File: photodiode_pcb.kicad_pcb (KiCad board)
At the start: 2 copper layers, 11.7 x 30.2 mm, 15 parts, among them P1 CONN_01X04, U1 LTC2461, U3 SD100-13-23-222, U4 OPA381

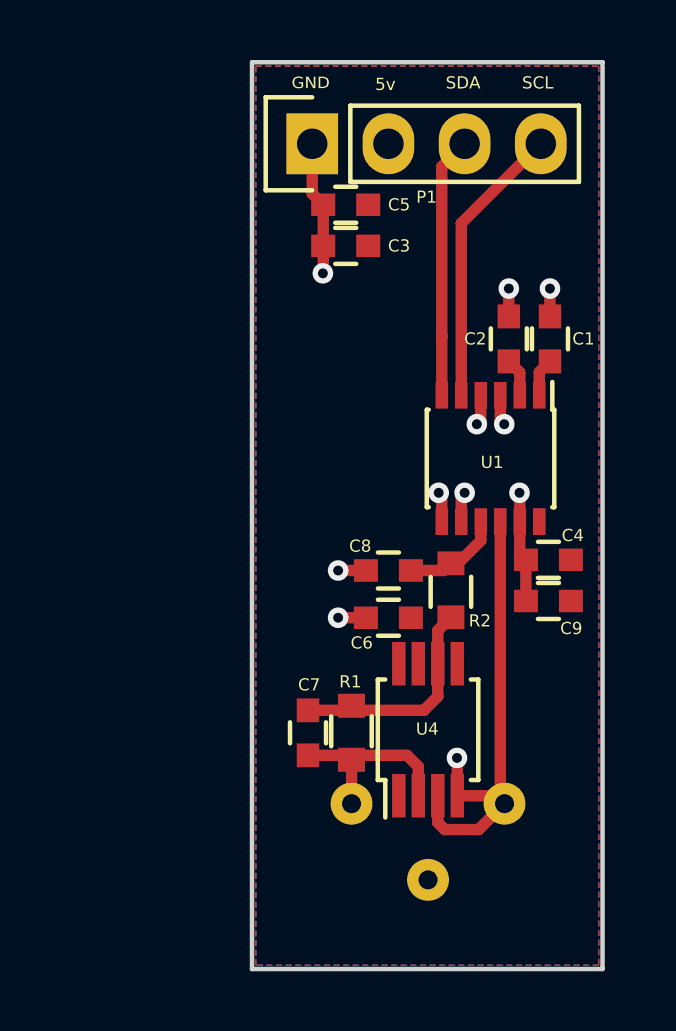
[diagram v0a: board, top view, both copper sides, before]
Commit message: Reorganize pcb and change footprints
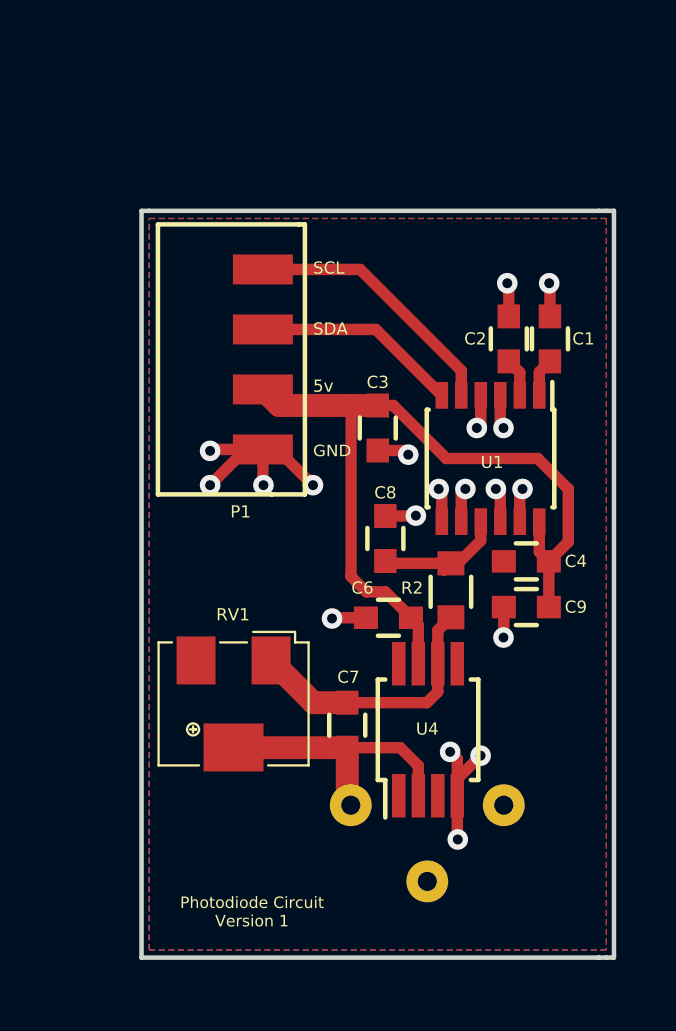
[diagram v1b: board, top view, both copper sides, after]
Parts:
- removed C5: .1u, Capacitors_SMD:C_0603
- removed R1: 10M, footprints:R_0603_smaller_handsolder
- added RV1: POT, footprints:BOURNS_3214W, F.Cu at (128.8, 103.4)
- C3: value 1u -> 10u
- P1: footprint Pin_Headers:Pin_Header_Straight_1x04 -> footprints:CONN_1x4_SMT_2mm
- moved P1 9.33 mm to (124.2, 93.3)
- moved C3 6.16 mm to (132.3, 95.6), turned to 90 degrees
- moved C7 1.33 mm to (131.3, 105.5)
- moved C8 1.07 mm to (132.6, 99.3), turned to 90 degrees
- moved C9 0.76 mm to (137.3, 101.6)
- moved C4 0.74 mm to (137.3, 100.1)
- moved U3 0.06 mm to (134.0, 108.2)
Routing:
- net VCC: track 0.00 -> 27.6 mm
- net GND: track 32.2 -> 25.8 mm, vias 11 -> 19
- net Net-(C7-Pad2): track 6.42 -> 9.58 mm
- net /SDA: track 8.70 -> 6.87 mm
- net Net-(C7-Pad1): track 7.33 -> 8.96 mm
- net /SCL: track 10.3 -> 8.83 mm
- net Net-(C8-Pad1): track 3.37 -> 4.79 mm
- added copper zone on F.Cu, net GND
- removed copper zone on F.Cu, net VCC
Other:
- board size 11.7 x 30.2 mm -> 15.7 x 24.9 mm
- board text added: "Photodiode Circuit Version 1"

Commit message: Reorganize project
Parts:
- P1: footprint footprints:CONN_1x4_SMT_2mm -> jnod_footprints:Sullins_M89_1X4
- R2: footprint footprints:R_0603_smaller_handsolder -> jnod_footprints:R_0603_smaller_handsolder
- RV1: value POT -> 2M; footprint footprints:BOURNS_3214W -> jnod_footprints:BOURNS_3214W
- U3: footprint footprints:SD100-13-23-222 -> jnod_footprints:TO-5-3
- moved P1 6.71 mm to (128.3, 98.7)
- moved C3 0.57 mm to (132.6, 96.1)
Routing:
- net VCC: track 27.6 -> 26.5 mm
- net GND: track 25.8 -> 25.0 mm, vias 19 -> 21
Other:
- board size 15.7 x 24.9 mm -> 18.2 x 25 mm
- board text added: "5vSCL"
- board text added: "5vSDA"
- board text added: "Digital Photodiode Version 1"
- board text added: "Gain Adjustment"
- board text removed: "Photodiode Circuit Version 1"
- board text removed: "SCL"
- board text removed: "SDA"

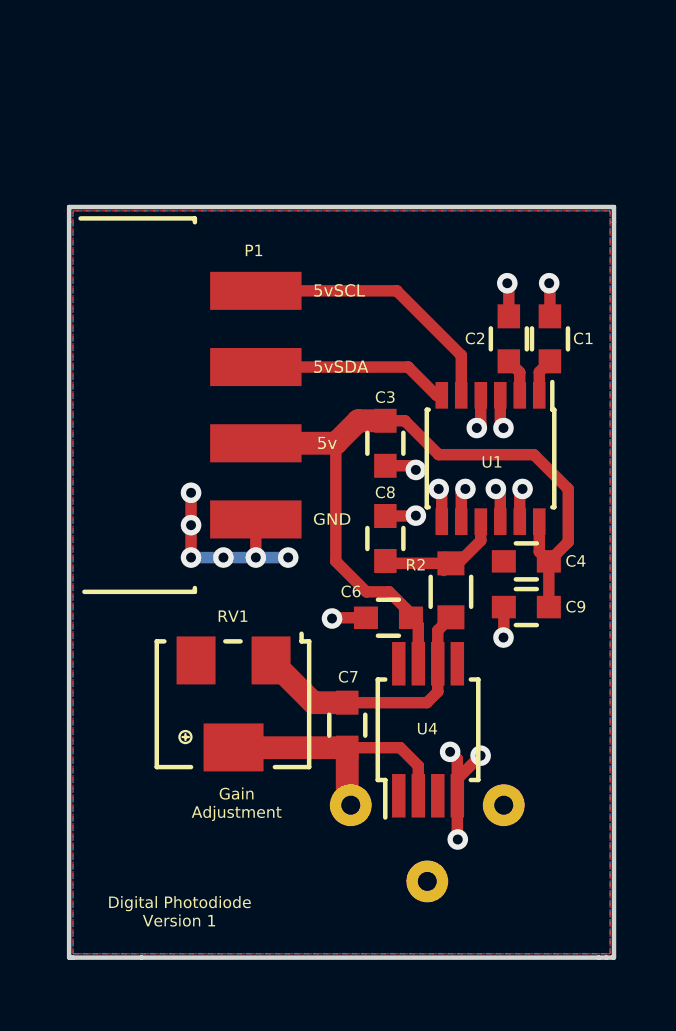
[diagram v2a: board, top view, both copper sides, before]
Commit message: Update footprints
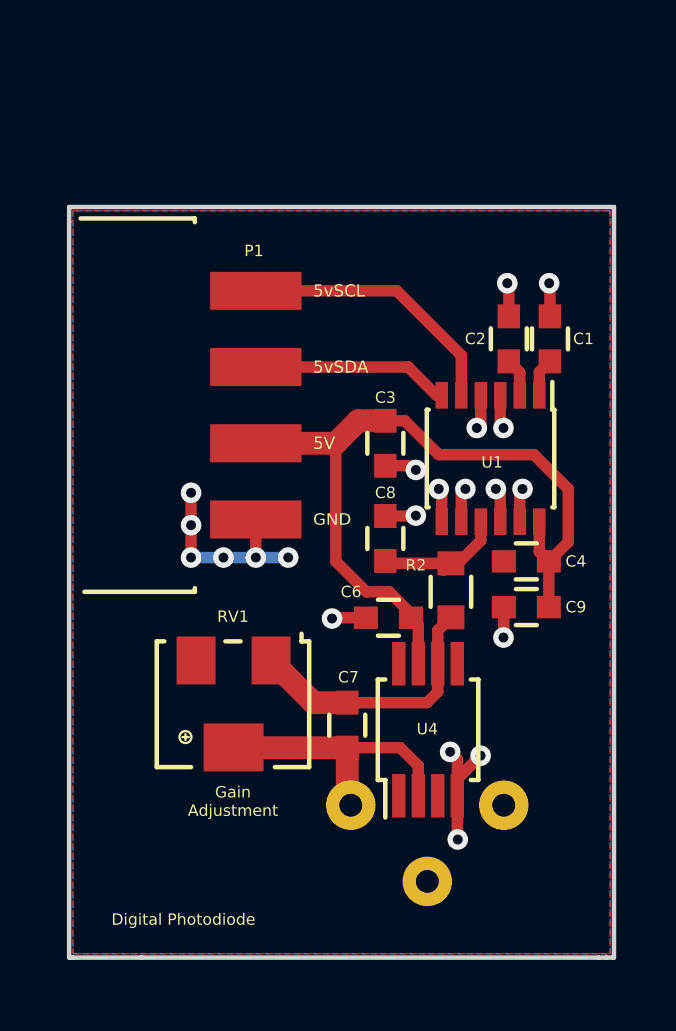
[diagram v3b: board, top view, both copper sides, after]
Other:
- board text added: "5V"
- board text added: "Digital Photodiode"
- board text removed: "5v"
- board text removed: "Digital Photodiode Version 1"
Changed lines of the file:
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@@
   )
   (setup
-    (last_trace_width 0.381)
+    (last_trace_width 0.1524)
     (user_trace_width 0.381)
     (user_trace_width 0.762)
@@
     )
   )
-  (module jnod_footprints:TO-5-3 (layer B.Cu)
-    (at 133.985 108.204 180)
-    (descr "TO-5,  3Pin,")
-    (tags "TO-5,  3Pin, TO-5-3")
-    (fp_text reference U3 (at -0.0254 -0.254 180) (layer B.SilkS)
-      (effects (font (size 0.381 0.381) (thickness 0.0762)) (justify mirror))
-    )
-    (fp_text value SD100-13-23-222 (at -0.0254 -4.064 180) (layer B.Fab)
-      (effects (font (size 0.381 0.381) (thickness 0.0762)) (justify mirror))
-    )
-    (fp_line (start -4.064 4.064) (end -3.81 4.318) (layer B.SilkS) (width 0.15))
-    (fp_line (start -3.81 4.318) (end -3.048 3.556) (layer B.SilkS) (width 0.15))
-    (fp_line (start -4.064 4.064) (end -4.318 3.81) (layer B.SilkS) (width 0.15))
-    (fp_line (start -4.318 3.81) (end -3.556 3.048) (layer B.SilkS) (width 0.15))
-    (fp_circle (center 0 0) (end 2.55 0) (layer B.SilkS) (width 0.15))
-    (fp_circle (center 0 0) (end 4.2 0) (layer B.SilkS) (width 0.15))
-    (fp_circle (center 0 0) (end 4.7 0) (layer B.SilkS) (width 0.15))
-    (pad 1 thru_hole circle (at -2.55 0 180) (size 1.397 1.397) (drill 0.635) (layers *.Cu *.Mask B.SilkS)
-      (net 1 GND))
-    (pad 2 thru_hole circle (at 0 -2.54 180) (size 1.397 1.397) (drill 0.635) (layers *.Cu *.Mask B.SilkS))
-    (pad 3 thru_hole circle (at 2.55 0 180) (size 1.397 1.397) (drill 0.635) (layers *.Cu *.Mask B.SilkS)
-      (net 4 "Net-(C7-Pad2)"))
-  )
   (module jnod_footprints:Sullins_M89_1X4 (layer F.Cu)
     (at 128.27 98.679 90)
@@
     (pad 3 smd rect (at 0 2.5 90) (size 1.6 1.3) (layers F.Cu F.Paste F.Mask))
   )
-  (gr_text "Gain\nAdjustment" (at 127.635 108.1405) (layer F.SilkS)
+  (module jnod_footprints:TO-5-3 (layer B.Cu)
+    (at 133.985 108.204 180)
+    (descr "TO-5,  3Pin,")
+    (tags "TO-5,  3Pin, TO-5-3")
+    (fp_text reference U3 (at -0.0254 -0.254 180) (layer B.SilkS)
+      (effects (font (size 0.4064 0.4064) (thickness 0.08128)) (justify mirror))
+    )
+    (fp_text value SD100-13-23-222 (at -0.0254 -4.064 180) (layer B.Fab)
+      (effects (font (size 0.4064 0.4064) (thickness 0.08128)) (justify mirror))
+    )
+    (fp_line (start -4.064 4.064) (end -3.81 4.318) (layer B.SilkS) (width 0.15))
+    (fp_line (start -3.81 4.318) (end -3.048 3.556) (layer B.SilkS) (width 0.15))
+    (fp_line (start -4.064 4.064) (end -4.318 3.81) (layer B.SilkS) (width 0.15))
+    (fp_line (start -4.318 3.81) (end -3.556 3.048) (layer B.SilkS) (width 0.15))
+    (fp_circle (center 0 0) (end 2.55 0) (layer B.SilkS) (width 0.15))
+    (fp_circle (center 0 0) (end 4.2 0) (layer B.SilkS) (width 0.15))
+    (fp_circle (center 0 0) (end 4.7 0) (layer B.SilkS) (width 0.15))
+    (pad 1 thru_hole circle (at -2.55 0 180) (size 1.651 1.651) (drill 0.762) (layers *.Cu *.Mask B.SilkS)
+      (net 1 GND))
+    (pad 2 thru_hole circle (at 0 -2.54 180) (size 1.651 1.651) (drill 0.762) (layers *.Cu *.Mask B.SilkS))
+    (pad 3 thru_hole circle (at 2.55 0 180) (size 1.651 1.651) (drill 0.762) (layers *.Cu *.Mask B.SilkS)
+      (net 4 "Net-(C7-Pad2)"))
+  )
+  (gr_text "Gain\nAdjustment" (at 127.508 108.077) (layer F.SilkS)
     (effects (font (size 0.381 0.381) (thickness 0.0762)))
   )
@@
   (gr_line (start 122.174 113.284) (end 122.047 113.284) (angle 90) (layer Edge.Cuts) (width 0.15))
   (gr_line (start 124.46 113.284) (end 122.174 113.284) (angle 90) (layer Edge.Cuts) (width 0.15))
-  (gr_text "Digital Photodiode\nVersion 1" (at 125.73 111.76) (layer F.SilkS)
+  (gr_text "Digital Photodiode" (at 125.857 112.014) (layer F.SilkS)
     (effects (font (size 0.381 0.381) (thickness 0.0762)))
   )
@@
     (effects (font (size 0.4064 0.4064) (thickness 0.08128)) (justify left))
   )
-  (gr_text 5v (at 130.302 96.139) (layer F.SilkS)
+  (gr_text 5V (at 130.175 96.139) (layer F.SilkS)
     (effects (font (size 0.4064 0.4064) (thickness 0.08128)) (justify left))
   )

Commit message: Update silk screen
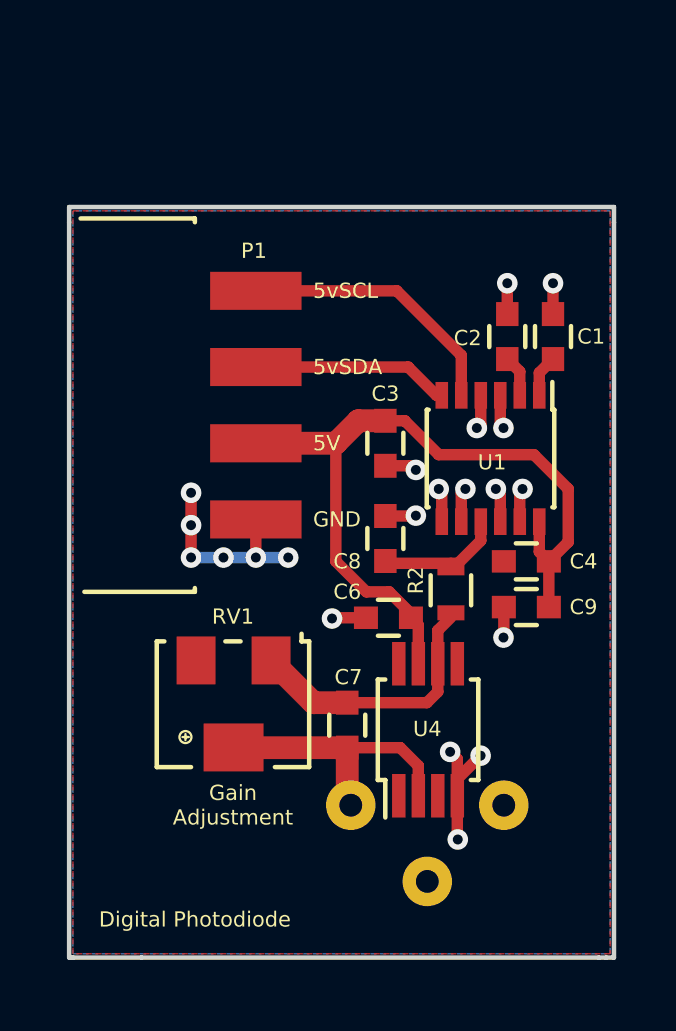
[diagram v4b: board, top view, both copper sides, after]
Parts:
- R2: footprint jnod_footprints:R_0603_smaller_handsolder -> Resistors_SMD:R_0603
- moved C1 0.13 mm to (138.2, 92.6)
- moved C2 0.09 mm to (136.7, 92.6)
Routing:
- net Net-(C8-Pad1): track 4.79 -> 4.16 mm

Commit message: Update footprint
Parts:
- removed U3: SD100-13-23-222, jnod_footprints:TO-5-3
- added D1: photodiode_asc, jnod_footprints:TO-5-3, B.Cu at (134.0, 108.2)
- C9: value 1u -> 10u
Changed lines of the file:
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@@
   )
   (setup
-    (last_trace_width 0.381)
+    (last_trace_width 0.762)
     (user_trace_width 0.381)
     (user_trace_width 0.762)
@@
     (pad_drill 0.762)
     (pad_to_mask_clearance 0)
+    (pad_to_paste_clearance -0.0254)
+    (pad_to_paste_clearance_ratio -0.02)
     (aux_axis_origin 0 0)
     (visible_elements FFFFFF7F)
     (pcbplotparams
-      (layerselection 0x010f0_80000001)
+      (layerselection 0x01008_00000000)
       (usegerberextensions false)
       (excludeedgelayer true)
@@
       (drillshape 0)
       (scaleselection 1)
-      (outputdirectory gerber/))
+      (outputdirectory photodiode_pcb_stencil/))
   )
   (net 0 "")
@@
       (effects (font (size 0.508 0.508) (thickness 0.127)))
     )
-    (fp_text value 1u (at 0 -0.0762 180) (layer F.Fab)
+    (fp_text value 10u (at 0 -0.0762 180) (layer F.Fab)
       (effects (font (size 0.508 0.508) (thickness 0.127)))
     )
@@
     (pad 3 smd rect (at 0 2.5 90) (size 1.6 1.3) (layers F.Cu F.Paste F.Mask))
   )
-  (module jnod_footprints:TO-5-3 (layer B.Cu)
-    (at 133.985 108.204 180)
-    (descr "TO-5,  3Pin,")
-    (tags "TO-5,  3Pin, TO-5-3")
-    (fp_text reference U3 (at -0.0254 -0.254 180) (layer B.SilkS)
-      (effects (font (size 0.508 0.508) (thickness 0.127)) (justify mirror))
-    )
-    (fp_text value SD100-13-23-222 (at -0.0254 -4.064 180) (layer B.Fab)
-      (effects (font (size 0.508 0.508) (thickness 0.127)) (justify mirror))
-    )
-    (fp_line (start -4.064 4.064) (end -3.81 4.318) (layer B.SilkS) (width 0.15))
-    (fp_line (start -3.81 4.318) (end -3.048 3.556) (layer B.SilkS) (width 0.15))
-    (fp_line (start -4.064 4.064) (end -4.318 3.81) (layer B.SilkS) (width 0.15))
-    (fp_line (start -4.318 3.81) (end -3.556 3.048) (layer B.SilkS) (width 0.15))
-    (fp_circle (center 0 0) (end 2.55 0) (layer B.SilkS) (width 0.15))
-    (fp_circle (center 0 0) (end 4.2 0) (layer B.SilkS) (width 0.15))
-    (fp_circle (center 0 0) (end 4.7 0) (layer B.SilkS) (width 0.15))
-    (pad 1 thru_hole circle (at -2.55 0 180) (size 1.651 1.651) (drill 0.762) (layers *.Cu *.Mask B.SilkS)
-      (net 1 GND))
-    (pad 2 thru_hole circle (at 0 -2.54 180) (size 1.651 1.651) (drill 0.762) (layers *.Cu *.Mask B.SilkS)
-      (clearance 0.381))
-    (pad 3 thru_hole circle (at 2.55 0 180) (size 1.651 1.651) (drill 0.762) (layers *.Cu *.Mask B.SilkS)
-      (net 4 "Net-(C7-Pad2)"))
-  )
   (module Resistors_SMD:R_0603 (layer F.Cu)
     (at 134.7724 101.0412 90)
@@
     )
   )
+  (module jnod_footprints:TO-5-3 (layer B.Cu)
+    (at 133.985 108.204 180)
+    (descr "TO-5,  3Pin,")
+    (tags "TO-5,  3Pin, TO-5-3")
+    (fp_text reference D1 (at 0 5.334 180) (layer B.SilkS)
+      (effects (font (size 0.4064 0.4064) (thickness 0.08128)) (justify mirror))
+    )
+    (fp_text value photodiode_asc (at -0.0254 -4.064 180) (layer B.Fab)
+      (effects (font (size 0.4064 0.4064) (thickness 0.08128)) (justify mirror))
+    )
+    (fp_line (start -4.064 4.064) (end -3.81 4.318) (layer B.SilkS) (width 0.15))
+    (fp_line (start -3.81 4.318) (end -3.048 3.556) (layer B.SilkS) (width 0.15))
+    (fp_line (start -4.064 4.064) (end -4.318 3.81) (layer B.SilkS) (width 0.15))
+    (fp_line (start -4.318 3.81) (end -3.556 3.048) (layer B.SilkS) (width 0.15))
+    (fp_circle (center 0 0) (end 2.55 0) (layer B.SilkS) (width 0.15))
+    (fp_circle (center 0 0) (end 4.2 0) (layer B.SilkS) (width 0.15))
+    (fp_circle (center 0 0) (end 4.7 0) (layer B.SilkS) (width 0.15))
+    (pad 1 thru_hole circle (at -2.55 0 180) (size 1.651 1.651) (drill 0.762) (layers *.Cu *.Mask B.SilkS)
+      (net 1 GND))
+    (pad 2 thru_hole circle (at 0 -2.54 180) (size 1.651 1.651) (drill 0.762) (layers *.Cu *.Mask B.SilkS)
+      (clearance 0.381))
+    (pad 3 thru_hole circle (at 2.55 0 180) (size 1.651 1.651) (drill 0.762) (layers *.Cu *.Mask B.SilkS)
+      (net 4 "Net-(C7-Pad2)"))
+  )
   (gr_text "Gain\nAdjustment" (at 127.508 108.204) (layer F.SilkS)
     (effects (font (size 0.508 0.508) (thickness 0.127)))
@@
     (effects (font (size 0.508 0.508) (thickness 0.127)) (justify left))
   )
-  (segment (start 138.176 91.833) (end 138.176 90.805) (width 0.381) (layer F.Cu) (net 1) (status 400000))
+  (segment (start 138.176 91.833) (end 138.176 90.805) (width 0.381) (layer F.Cu) (net 1))
   (via (at 138.176 90.805) (size 0.6858) (drill 0.3302) (layers F.Cu B.Cu) (net 1))
-  (segment (start 136.652 91.833) (end 136.652 90.805) (width 0.381) (layer F.Cu) (net 1) (status 400000))
+  (segment (start 136.652 91.833) (end 136.652 90.805) (width 0.381) (layer F.Cu) (net 1))
   (via (at 136.652 90.805) (size 0.6858) (drill 0.3302) (layers F.Cu B.Cu) (net 1))
   (segment (start 126.111 97.79) (end 126.111 98.8695) (width 0.381) (layer F.Cu) (net 1))
@@
   (segment (start 135.7682 99.385) (end 135.012 100.1412) (width 0.381) (layer F.Cu) (net 5))
   (segment (start 135.012 100.1412) (end 134.7724 100.1412) (width 0.381) (layer F.Cu) (net 5))
-  (segment (start 137.7182 94.542) (end 137.7182 93.7908) (width 0.381) (layer F.Cu) (net 6) (status 400000))
-  (segment (start 137.7182 93.7908) (end 138.176 93.333) (width 0.381) (layer F.Cu) (net 6) (status 800000))
-  (segment (start 137.0682 94.542) (end 137.0682 93.7492) (width 0.381) (layer F.Cu) (net 7) (status 400000))
-  (segment (start 137.0682 93.7492) (end 136.652 93.333) (width 0.381) (layer F.Cu) (net 7) (status 800000))
+  (segment (start 137.7182 94.542) (end 137.7182 93.7908) (width 0.381) (layer F.Cu) (net 6))
+  (segment (start 137.7182 93.7908) (end 138.176 93.333) (width 0.381) (layer F.Cu) (net 6))
+  (segment (start 137.0682 94.542) (end 137.0682 93.7492) (width 0.381) (layer F.Cu) (net 7))
+  (segment (start 137.0682 93.7492) (end 136.652 93.333) (width 0.381) (layer F.Cu) (net 7))
   (segment (start 134.4682 94.542) (end 134.293 94.542) (width 0.381) (layer F.Cu) (net 8))
   (segment (start 134.293 94.542) (end 133.35 93.599) (width 0.381) (layer F.Cu) (net 8))
